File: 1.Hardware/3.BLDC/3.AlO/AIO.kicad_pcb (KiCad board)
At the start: 4 copper layers, 63.1 x 63.5 mm, 157 parts, among them IC1 FD6288Q, IC2 FD6288Q, J1 FLY_WHEEL, J2 SWD&UART, J3 MOTOR_BACK, J4 MR30, J5 MR30, J6 Hall, J7 Hall, J8 MOTOR, J9 MOTOR, Q1 NMOS, Q10 NMOS, Q11 NMOS, Q12 NMOS, Q2 NMOS, Q3 NMOS, Q4 NMOS, Q5 NMOS, Q6 NMOS, Q7 NMOS, Q8 NMOS, Q9 NMOS, SW1 SW_SPDT, SW2 SW_SPDT, U2 RT9013-33GB, U3 ME3116, Y1 8MHz

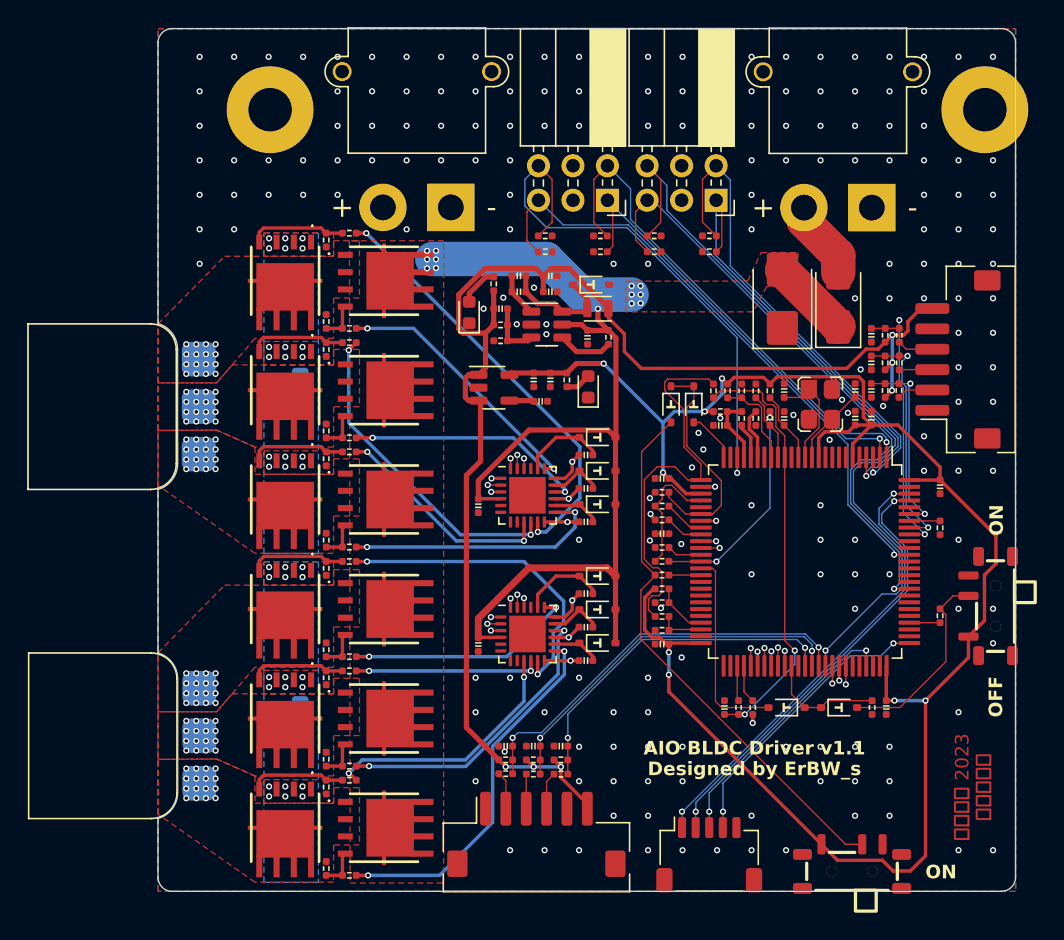
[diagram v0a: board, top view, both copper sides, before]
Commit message: Update 3D model to v1.2
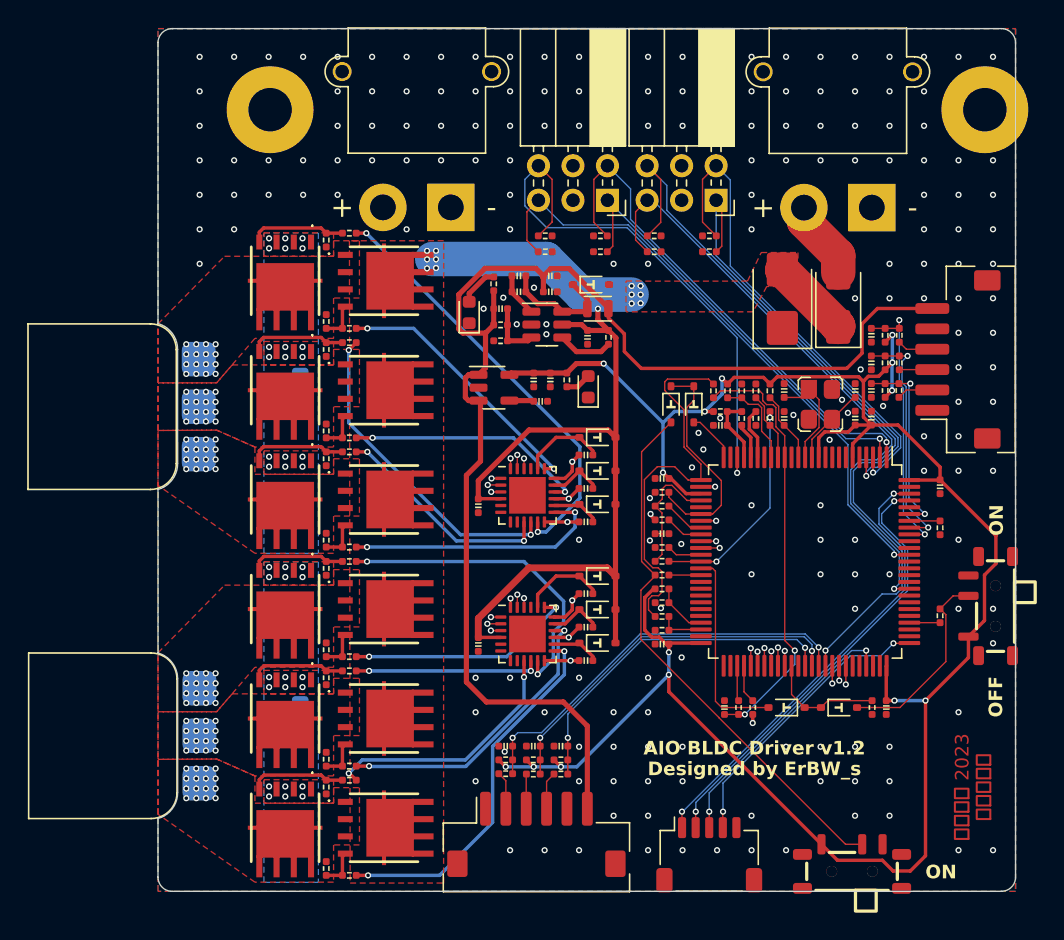
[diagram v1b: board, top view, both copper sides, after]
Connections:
- R64 pad 1: +5V -> +3.3V
- R65 pad 1: +5V -> +3.3V
- R66 pad 1: +5V -> +3.3V
- R67 pad 1: +5V -> +3.3V
- R68 pad 1: +5V -> +3.3V
- R69 pad 1: +5V -> +3.3V
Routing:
- net +3.3V: track 133.9 -> 159.2 mm, vias 8 -> 14
- net +5V: track 102.2 -> 97.4 mm, vias 6 -> 0
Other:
- board text added: "AIO BLDC Driver v1.2"
- board text removed: "AIO BLDC Driver v1.1"
